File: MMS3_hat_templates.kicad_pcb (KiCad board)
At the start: 4 copper layers, 100 x 50 mm, 53 parts, among them J1 Chainbus in, J2 Chainbus Out, J3 Conn_01x04_Pin, J4 AMASS XT60 Male, J5 AMASS XT60 Female, J8 Conn_01x03_Pin, SW1 SW_DIP_x04, U1 SN74CB3Q3384APW, U2 M24C64, U4 AMS1117, U5 LM2596HVS-ADJRG

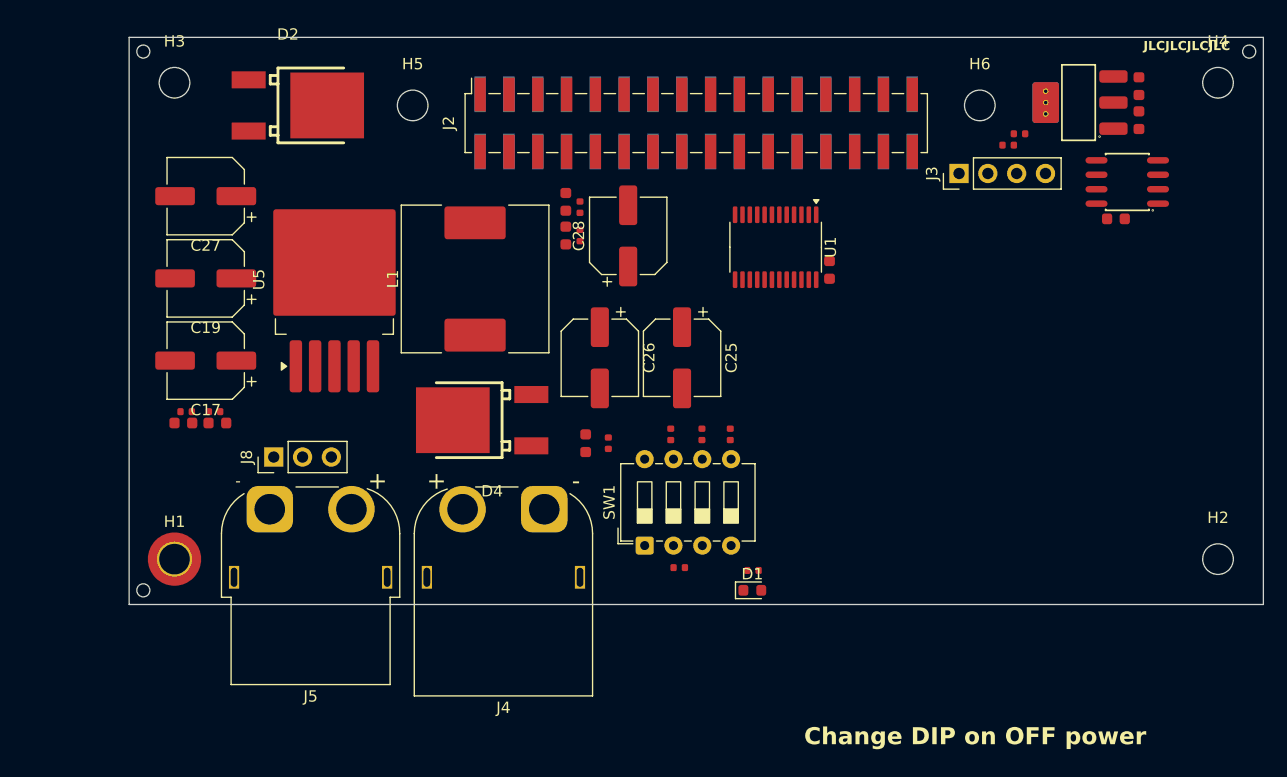
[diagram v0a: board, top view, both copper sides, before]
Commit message: updated XT60 place. added routing
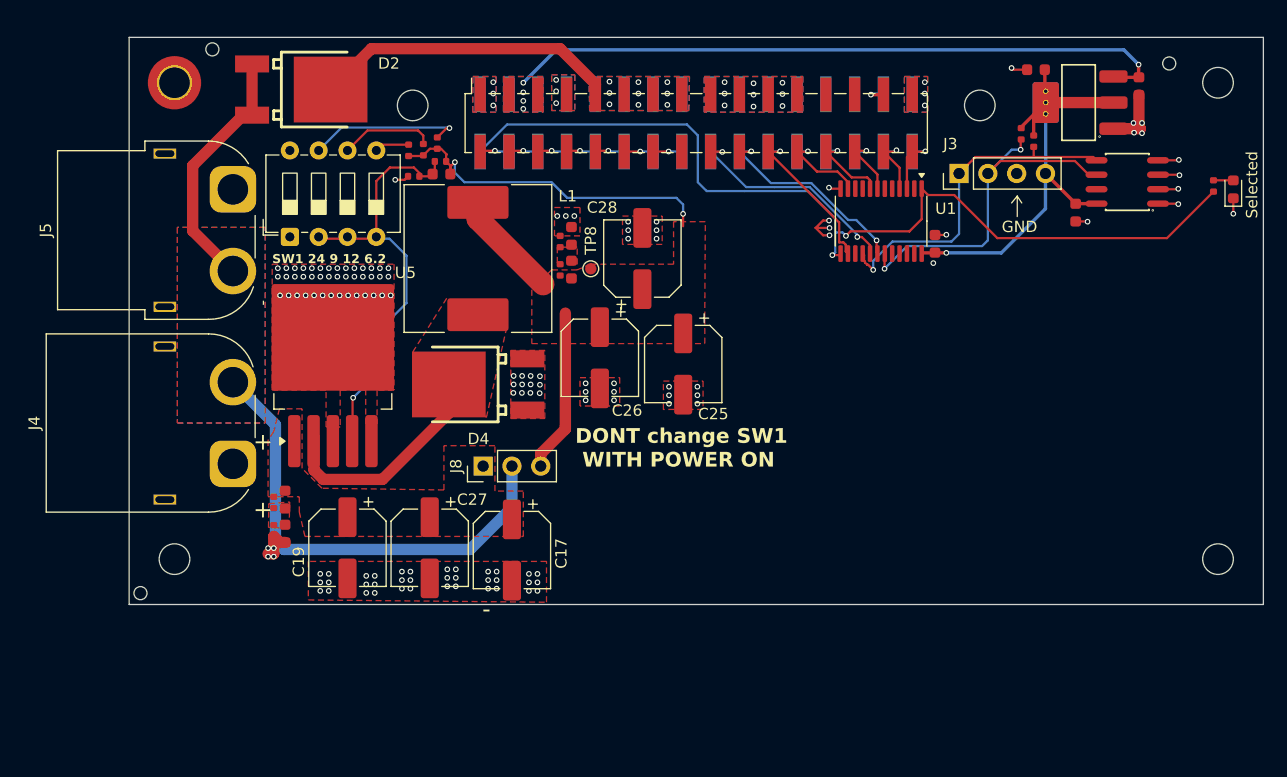
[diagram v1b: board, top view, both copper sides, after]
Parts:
- added TP8: TestPoint, TestPoint:TestPoint_Pad_D1.0mm, F.Cu at (118.7, 108.4)
- moved D1 55.2 mm to (175.3, 101.4), turned to 90 degrees
- moved R1 52.9 mm to (173.6, 101.1), turned to 90 degrees
- moved H1 42.0 mm to (82.0, 92.0)
- moved H3 42.0 mm to (82.0, 134.0)
- moved R12 41.7 mm to (103.1, 100.2), turned to 0 degrees
- moved SW1 41.5 mm to (92.2, 105.6)
- moved R16 37.8 mm to (102.6, 98.0), turned to -90 degrees
- moved C27 36.8 mm to (104.5, 133.0), turned to -90 degrees
- moved R15 35.1 mm to (103.9, 97.9), turned to -90 degrees
- moved R14 32.9 mm to (105.2, 97.3), turned to -90 degrees
- moved C17 31.7 mm to (111.8, 133.2), turned to -90 degrees
- moved R13 28.9 mm to (105.5, 98.9), turned to 0 degrees
- moved J5 28.4 mm to (87.2, 101.4), turned to 90 degrees
- moved J4 27.7 mm to (87.2, 125.6), turned to 90 degrees
- moved C22 26.9 mm to (105.5, 100.0), turned to 0 degrees
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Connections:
- U1 pad 10: unconnected-(U1-1B5-Pad10) -> /Bus_switch/Chainbus.SCK
- U1 pad 11: unconnected-(U1-1A5-Pad11) -> /Bus_switch/Chainbus_In.SCK
- U1 pad 16: /Bus_switch/Chainbus.SCK -> /Bus_switch/Chainbus.SDA
- U1 pad 17: /Bus_switch/Chainbus_In.SCK -> /Bus_switch/Chainbus_In.SDA
- U1 pad 18: /Bus_switch/Chainbus_In.MOSI -> /Bus_switch/Chainbus_In.SCL
- U1 pad 19: /Bus_switch/Chainbus.MOSI -> /Bus_switch/Chainbus.SCL
- U1 pad 2: /Bus_switch/Chainbus.SDA -> /Bus_switch/Chainbus.RX
- U1 pad 20: /Bus_switch/Chainbus.MISO -> unconnected-(U1-2B4-Pad20)
- U1 pad 21: /Bus_switch/Chainbus_In.MISO -> unconnected-(U1-2A4-Pad21)
- U1 pad 3: /Bus_switch/Chainbus_In.SDA -> /Bus_switch/Chainbus_In.RX
- U1 pad 4: /Bus_switch/Chainbus_In.SCL -> /Bus_switch/Chainbus_In.TX
- U1 pad 5: /Bus_switch/Chainbus.SCL -> /Bus_switch/Chainbus.TX
- U1 pad 6: /Bus_switch/Chainbus.TX -> /Bus_switch/Chainbus.MISO
- U1 pad 7: /Bus_switch/Chainbus_In.TX -> /Bus_switch/Chainbus_In.MISO
- U1 pad 8: /Bus_switch/Chainbus_In.RX -> /Bus_switch/Chainbus_In.MOSI
- U1 pad 9: /Bus_switch/Chainbus.RX -> /Bus_switch/Chainbus.MOSI
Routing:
- net /Bus_switch/SEL1: track 0.00 -> 82.6 mm, vias 0 -> 2
- net Vin: track 0.00 -> 64.3 mm
- net +5V: track 0.00 -> 59.4 mm, vias 0 -> 5
- net U_reg: track 0.00 -> 55.0 mm, vias 0 -> 2
- net +3V3: track 0.00 -> 40.9 mm, vias 0 -> 1
- net Net-(U5-FB): track 0.00 -> 38.3 mm, vias 0 -> 1
- net /Bus_switch/Chainbus.SCL: track 0.00 -> 32.6 mm, vias 0 -> 2
- net /Bus_switch/Chainbus.SDA: track 0.00 -> 30.3 mm, vias 0 -> 1
- net GND: track 0.00 -> 27.6 mm, vias 0 -> 151
- net BRD_VIN: track 0.00 -> 27.1 mm, vias 0 -> 9
- net Net-(D4-K): track 0.00 -> 21.4 mm
- net /Bus_switch/Chainbus_In.SDA: track 0.00 -> 20.4 mm, vias 0 -> 2
- net /Bus_switch/Chainbus_In.SCL: track 0.00 -> 18.6 mm, vias 0 -> 2
- net /Bus_switch/Chainbus_In.CS: track 0.00 -> 14.2 mm, vias 0 -> 1
- net Net-(R14-Pad1): track 0.00 -> 13.8 mm, vias 0 -> 1
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- added copper zone on B.Cu, net +5V
- added copper zone on F.Cu, net +5V
- added copper zone on B.Cu, net BRD_VIN
- added copper zone on F.Cu, net BRD_VIN
- added copper zone on B.Cu, net GND
- added copper zone on F.Cu, net GND
- added copper zone on In1.Cu, net GND
- added copper zone on In2.Cu, net GND
- added copper zone on F.Cu, net Net-(C20-Pad2)
- added copper zone on F.Cu, net Net-(C23-Pad2)
- added copper zone on F.Cu, net Net-(D4-K)
- added copper zone on F.Cu, net Net-(J8-Pin_1)
- added copper zone on F.Cu, net U_reg
- added copper zone on B.Cu, net Vin
- added copper zone on F.Cu, net Vin
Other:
- board text added: "All mounting holes Are M2.5"
- board text added: "DONT change SW1 WITH POWER ON"
- board text added: "SW1 24 9 12 6.2"
- board text added: "Selected"
- board text removed: "+"
- board text removed: "-"
- board text removed: "3V3"
- board text removed: "5V0"
- board text removed: "B G R C D 3"
- board text removed: "Change DIP on OFF power"
- board text removed: "Encloshure is supposed to have 2mm walls :)"
- board text removed: "FW VER. MC1"
- board text removed: "FW VER. MC2"
- board text removed: "G"
- board text removed: "IO R G"
- board text removed: "N/C"
- board text removed: "VIN"
- board text removed: "Ymin LKME5001J102MF"

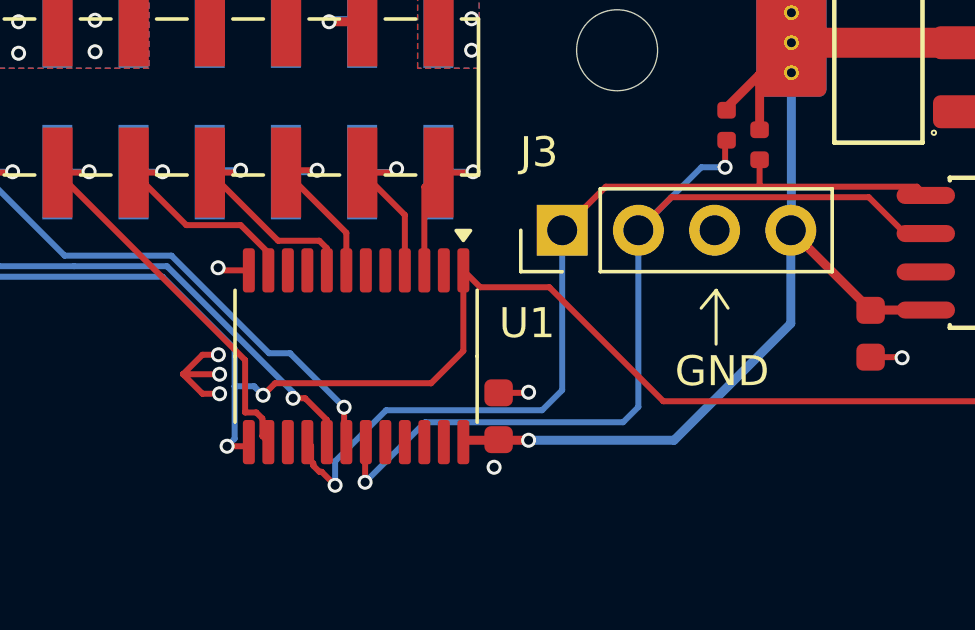
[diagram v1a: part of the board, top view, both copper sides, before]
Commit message: added pullup on bus switch negate OE
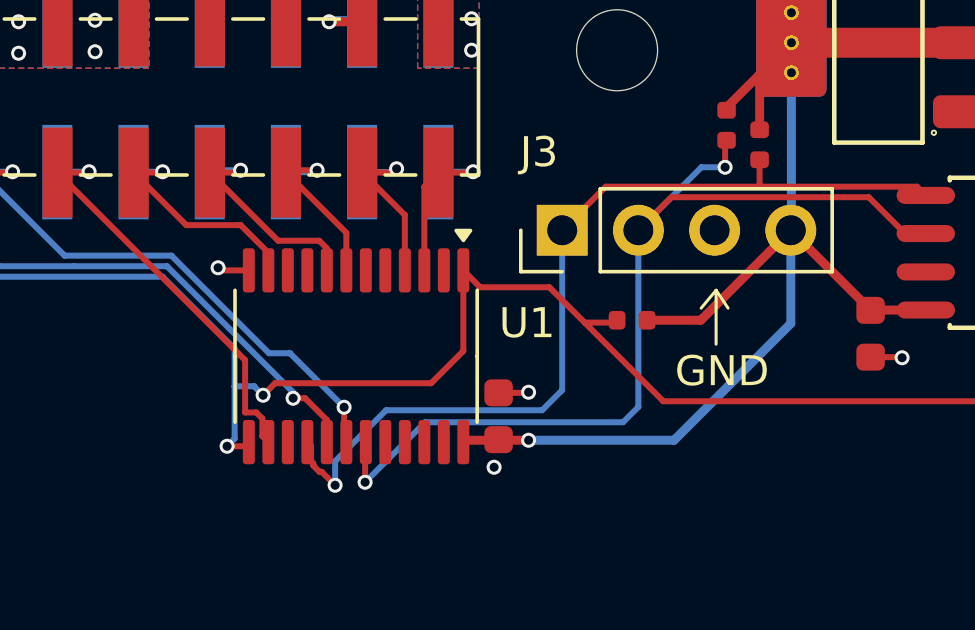
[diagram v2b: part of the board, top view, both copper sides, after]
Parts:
- added R4: 10kΩ, PCM_JLCPCB:R_0402, F.Cu at (153.5, 103.0)
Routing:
- net +3V3: track 40.9 -> 46.9 mm
- net GND: track 27.6 -> 23.4 mm, vias 151 -> 148
- net /Bus_switch/SEL1: track 82.6 -> 83.7 mm

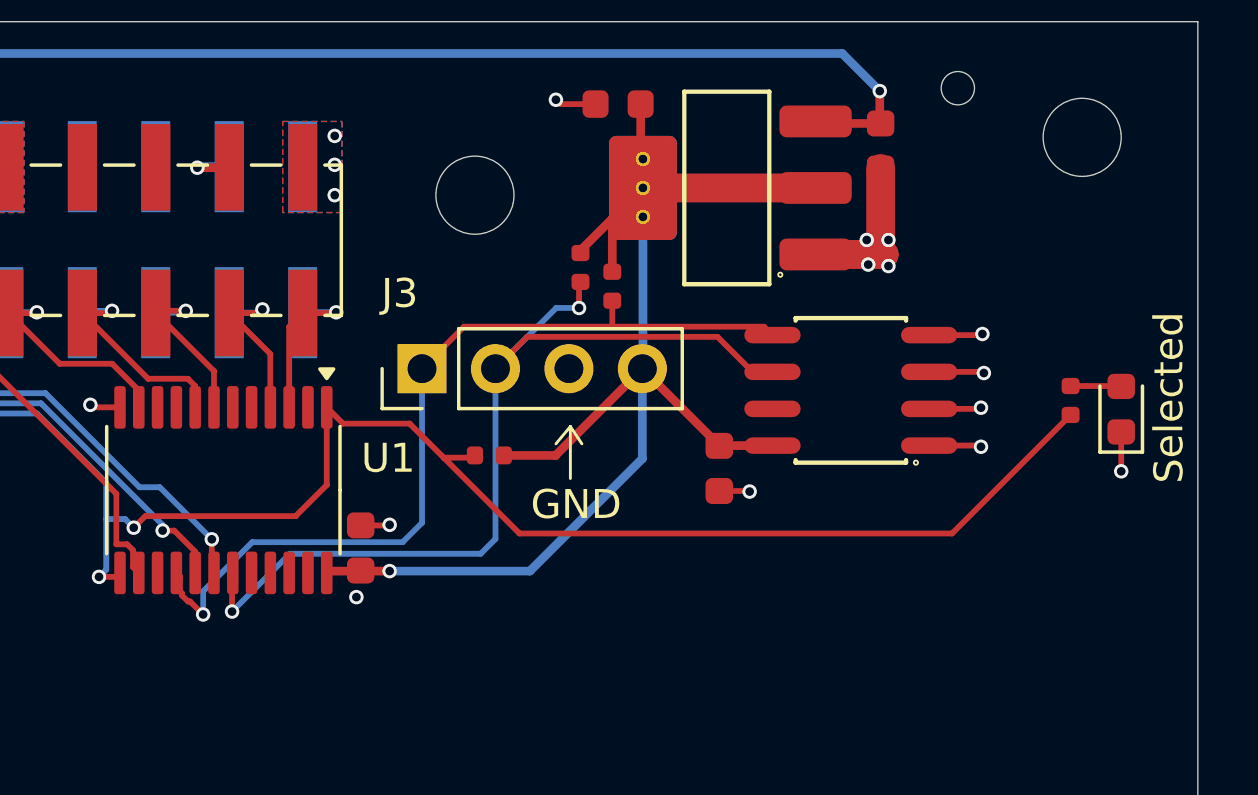
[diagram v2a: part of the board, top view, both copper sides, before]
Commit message: moved I2C header to the side
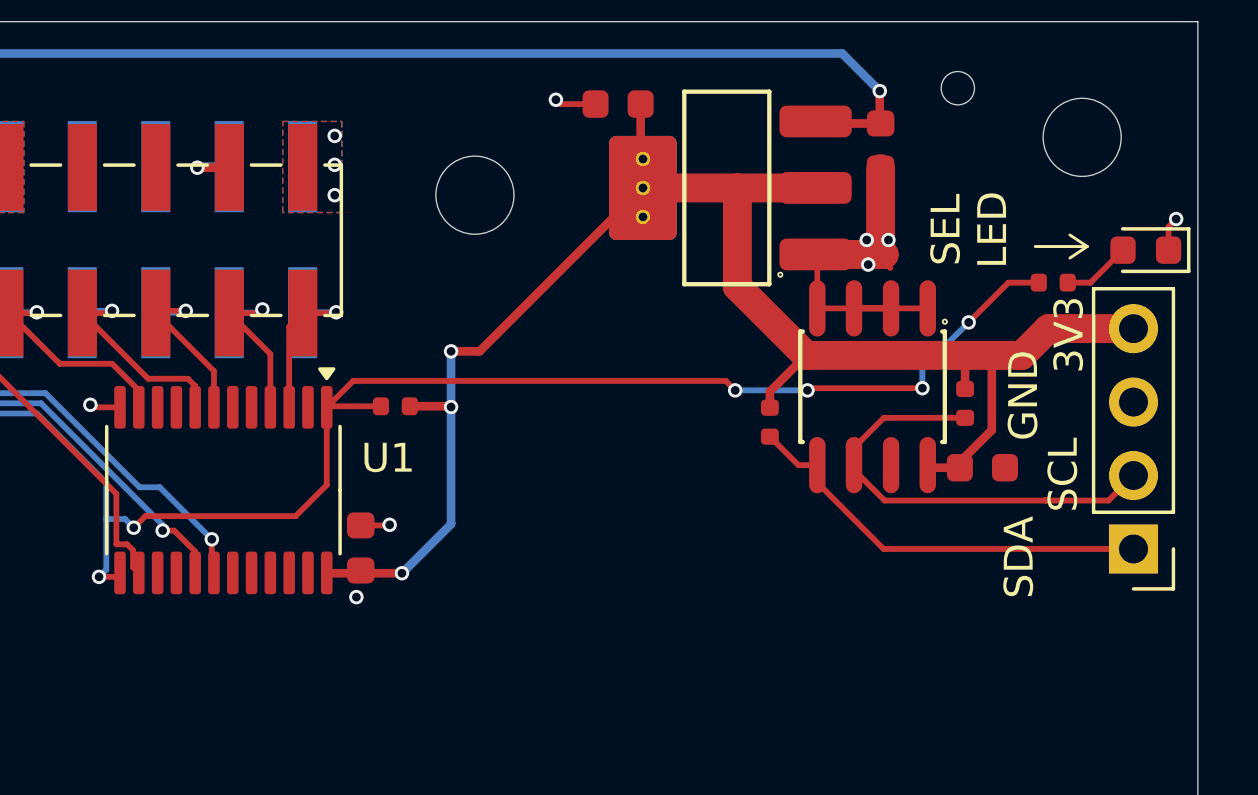
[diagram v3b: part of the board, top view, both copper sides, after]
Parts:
- moved G*** 60.5 mm to (165.8, 127.8)
- moved J3 25.4 mm to (175.8, 106.2), turned to 180 degrees
- moved R2 14.1 mm to (169.9, 101.2)
- moved C2 9.10 mm to (170.6, 103.4), turned to 0 degrees
- moved R3 7.20 mm to (163.2, 101.8)
- moved D1 5.57 mm to (176.2, 95.9), turned to 180 degrees
- moved R1 4.12 mm to (173.0, 97.0), turned to 0 degrees
- moved R4 3.67 mm to (150.2, 101.3)
- moved U2 0.76 mm to (166.8, 100.6), turned to 180 degrees
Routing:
- net /Bus_switch/Chainbus.SCL: track 32.6 -> 15.5 mm, vias 2 -> 0
- net /Bus_switch/Chainbus.SDA: track 30.3 -> 14.5 mm, vias 1 -> 0
- net +3V3: track 46.9 -> 57.0 mm, vias 1 -> 3
- net GND: track 23.4 -> 21.6 mm, vias 148 -> 142
- net /Bus_switch/SEL1: track 83.7 -> 82.3 mm, vias 2 -> 6
- net Net-(D1-A): track 1.52 -> 2.38 mm
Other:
- board text added: "3"
- board text added: "3V3"
- board text added: "SCL"
- board text added: "SDA"
- board text added: "SEL LED"
- board text removed: "2"
- board text removed: "Selected"
